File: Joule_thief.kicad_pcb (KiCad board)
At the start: 2 copper layers, 34 x 24 mm, 6 parts, among them P1 CONN_01X02, Q1 MMBT3904, T1 TRANSFORMER

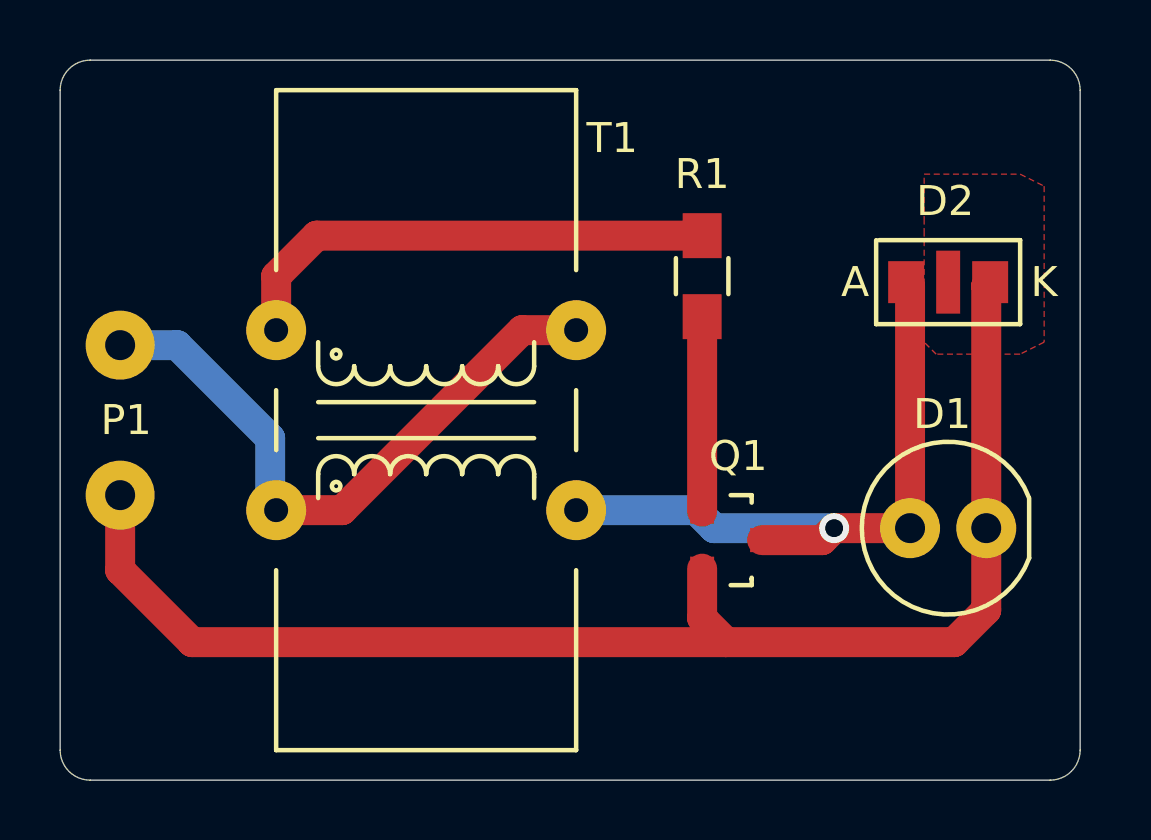
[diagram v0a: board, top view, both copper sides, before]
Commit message: Added test points, improved layout
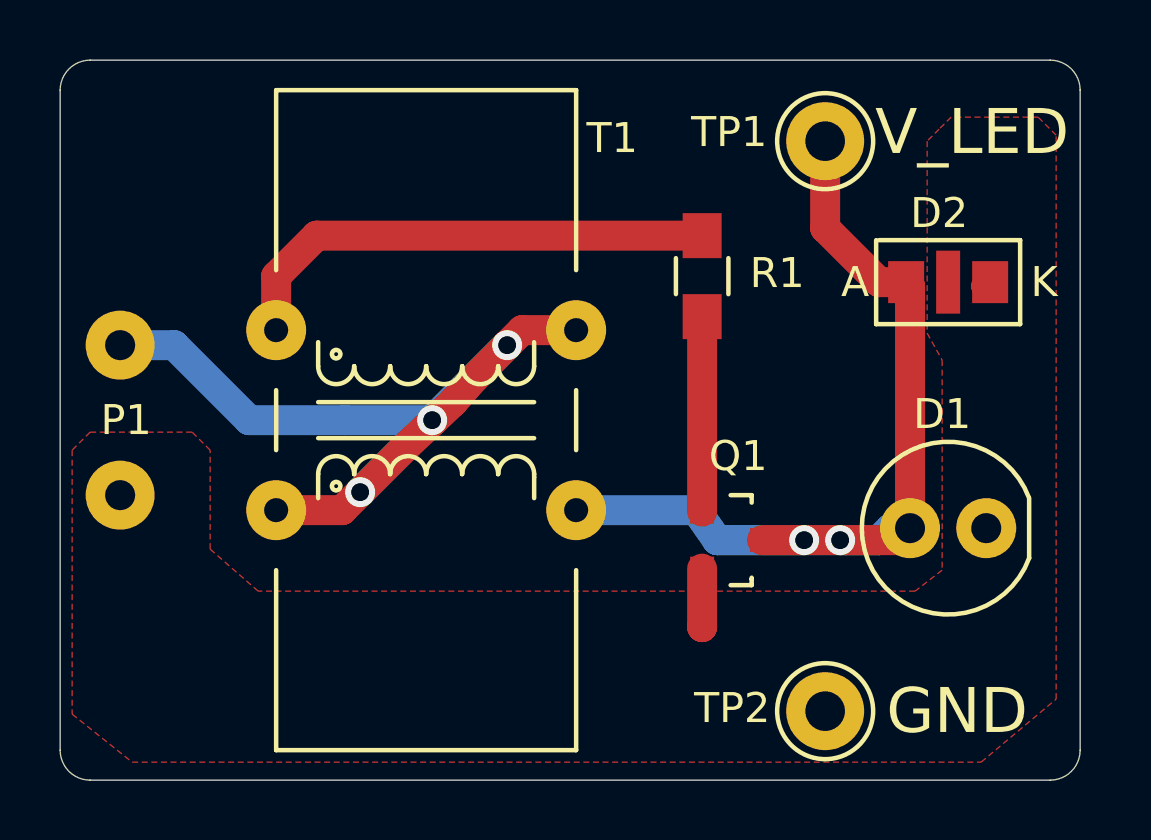
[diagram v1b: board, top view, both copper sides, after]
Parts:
- added TP1: Test_point_loop_1.32mm, nightmechanic_pcb:Test_point_glass_1.32, F.Cu at (161.5, 95.7)
- added TP2: Test_point_loop_1.32mm, nightmechanic_pcb:Test_point_glass_1.32, F.Cu at (161.5, 114.7)
- added VAL: REF, Logos:Gears_F.SilkS_10mm_flipped, B.Cu at (159.0, 106.0)
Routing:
- net Net-(D1-Pad1): track 46.8 -> 2.32 mm
- net Net-(D1-Pad2): track 22.2 -> 36.3 mm, vias 1 -> 2
- net Net-(P1-Pad2): track 21.3 -> 31.2 mm, vias 0 -> 3
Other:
- rule pad_to_mask_clearance: 0.2 -> 0.075
- board text added: "GND"
- board text added: "Simple Joule Thief"
- board text added: "V_LED"
- board text removed: "Joule Thief"
